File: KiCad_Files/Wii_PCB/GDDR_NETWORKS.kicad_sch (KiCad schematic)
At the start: 20 parts

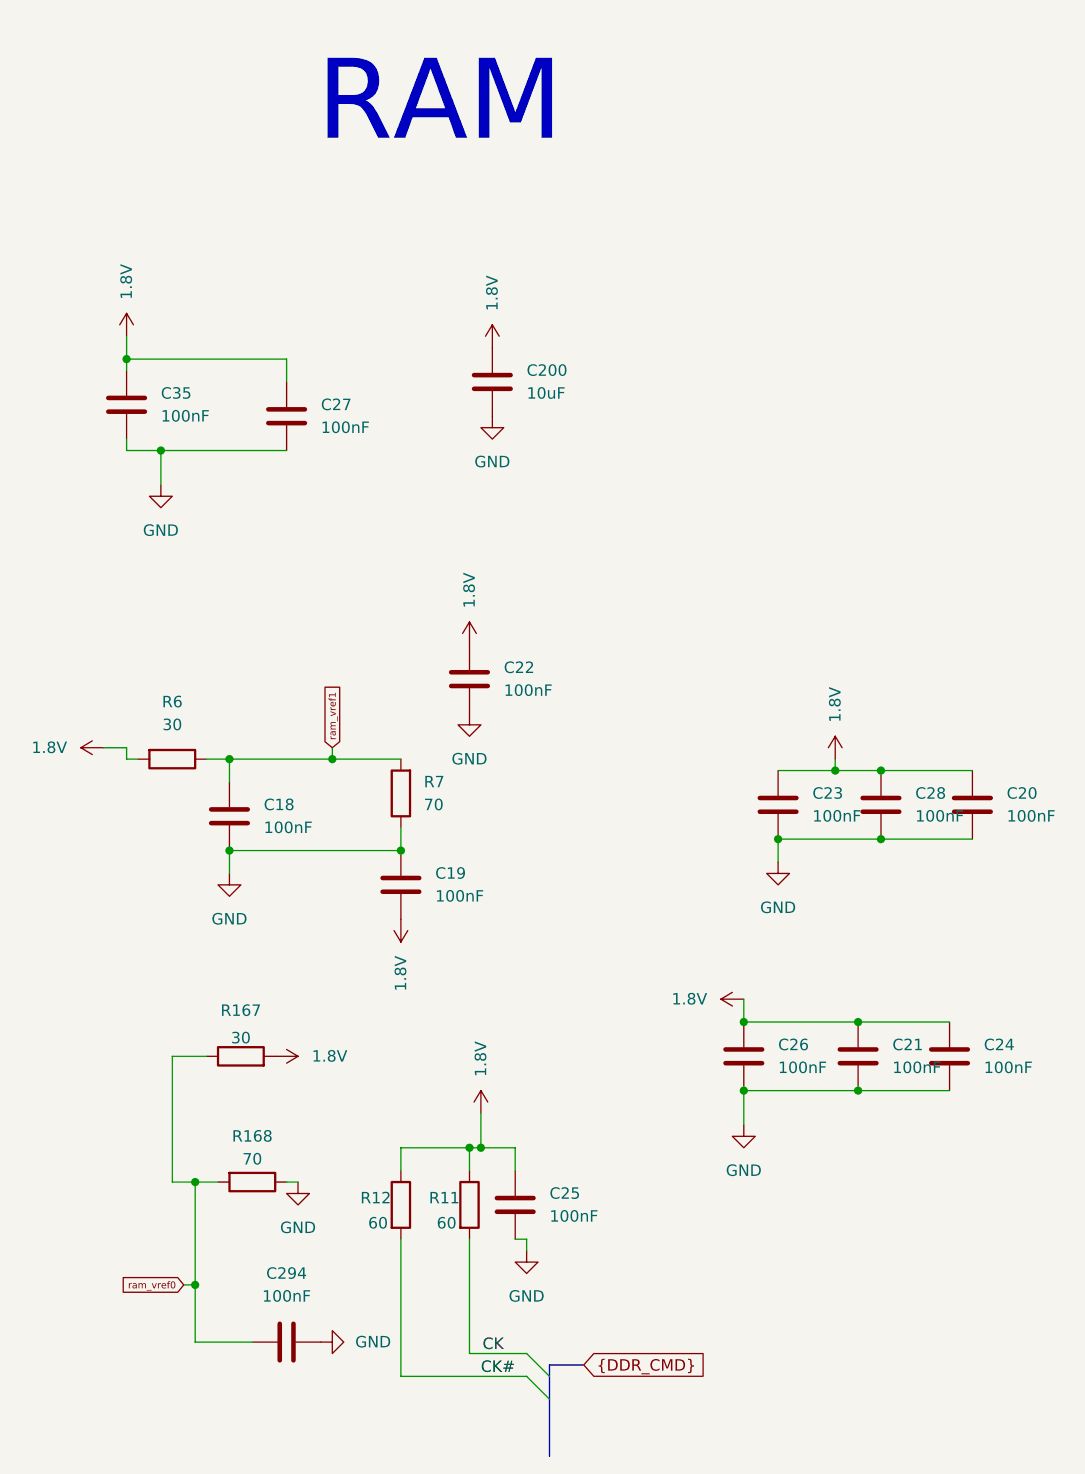
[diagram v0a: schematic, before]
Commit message: Updated RAM & GPU bus to allow custom net rules for measuring intra-track spacing, added pad for reset, removed debug pads, reorganized ram schematic to cluster length matched signals, changed MX chip and U10 symbols, and re-labeled the wifi net interface.
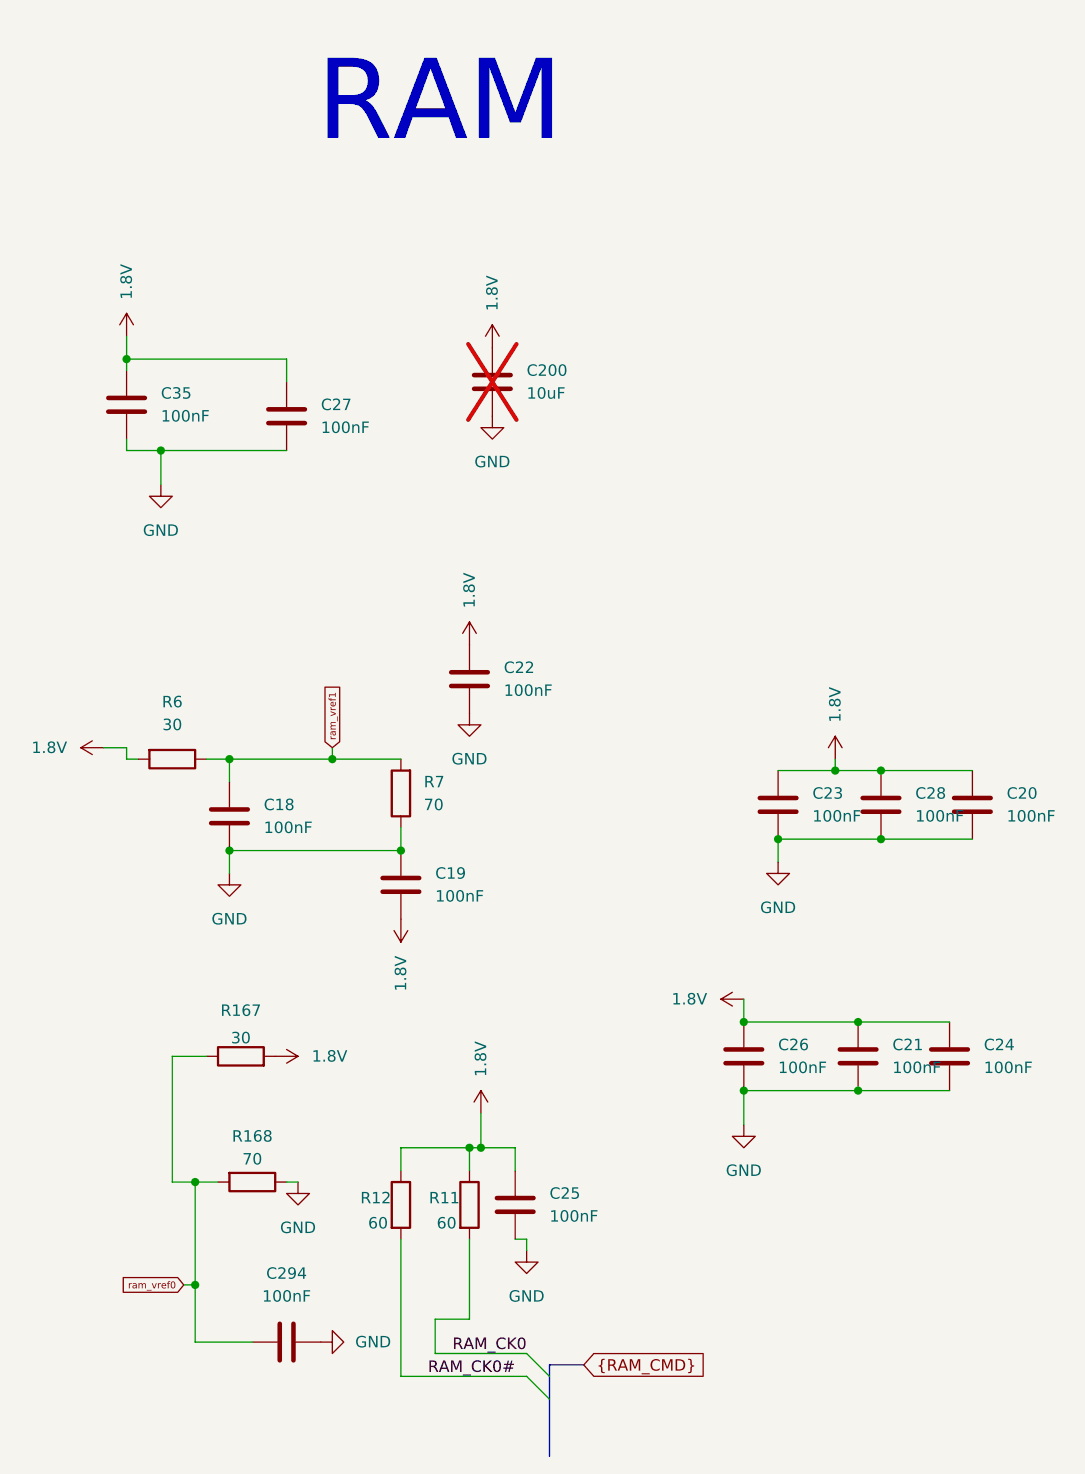
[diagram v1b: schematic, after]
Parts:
- C200: now not fitted; now left out of the parts list
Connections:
- net CK renamed RAM_CK0
- net CK# renamed RAM_CK0#
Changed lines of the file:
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@@
 	(wire
 		(pts
-			(xy 92.71 170.18) (xy 99.06 170.18)
+			(xy 88.9 170.18) (xy 99.06 170.18)
 		)
 		(stroke
@@
 	(wire
 		(pts
+			(xy 88.9 166.37) (xy 92.71 166.37)
+		)
+		(stroke
+			(width 0)
+			(type default)
+		)
+	)
+	(wire
+		(pts
 			(xy 138.43 105.41) (xy 148.59 105.41)
 		)
@@
 	(wire
 		(pts
-			(xy 92.71 157.48) (xy 92.71 170.18)
+			(xy 92.71 157.48) (xy 92.71 166.37)
 		)
 		(stroke
@@
 	(wire
 		(pts
+			(xy 88.9 170.18) (xy 88.9 166.37)
+		)
+		(stroke
+			(width 0)
+			(type default)
+		)
+	)
+	(wire
+		(pts
 			(xy 66.04 104.14) (xy 77.47 104.14)
 		)
@@
 		)
 	)
-	(label "CK"
-		(at 96.52 170.18 180)
+	(label "RAM_CK0"
+		(at 99.06 170.18 180)
 		(effects
 			(font
@@
 		)
 	)
-	(label "CK#"
+	(label "RAM_CK0#"
 		(at 97.79 172.72 180)
 		(effects
@@
 		)
 	)
-	(global_label "{DDR_CMD}"
+	(global_label "{RAM_CMD}"
 		(shape input)
 		(at 105.41 171.45 0)
@@
 		(unit 1)
 		(exclude_from_sim no)
-		(in_bom yes)
-		(on_board yes)
-		(dnp no)
+		(in_bom no)
+		(on_board no)
+		(dnp yes)
 		(fields_autoplaced yes)
 		(property "Reference" "C200"
